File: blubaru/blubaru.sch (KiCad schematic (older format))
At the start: 20 parts

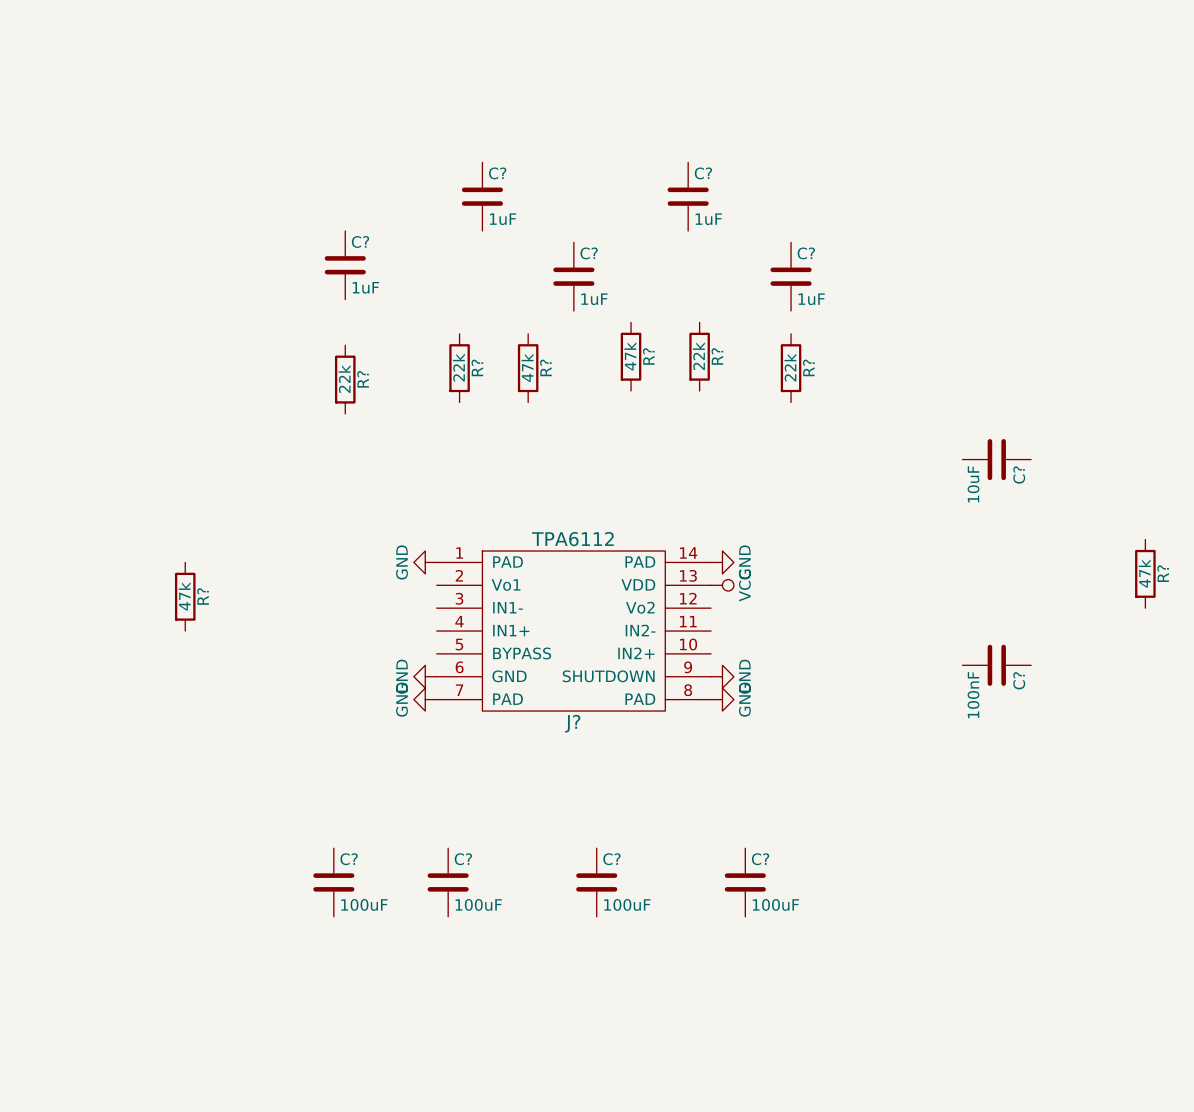
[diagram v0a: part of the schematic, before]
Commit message: Make connections to components on amplifier.
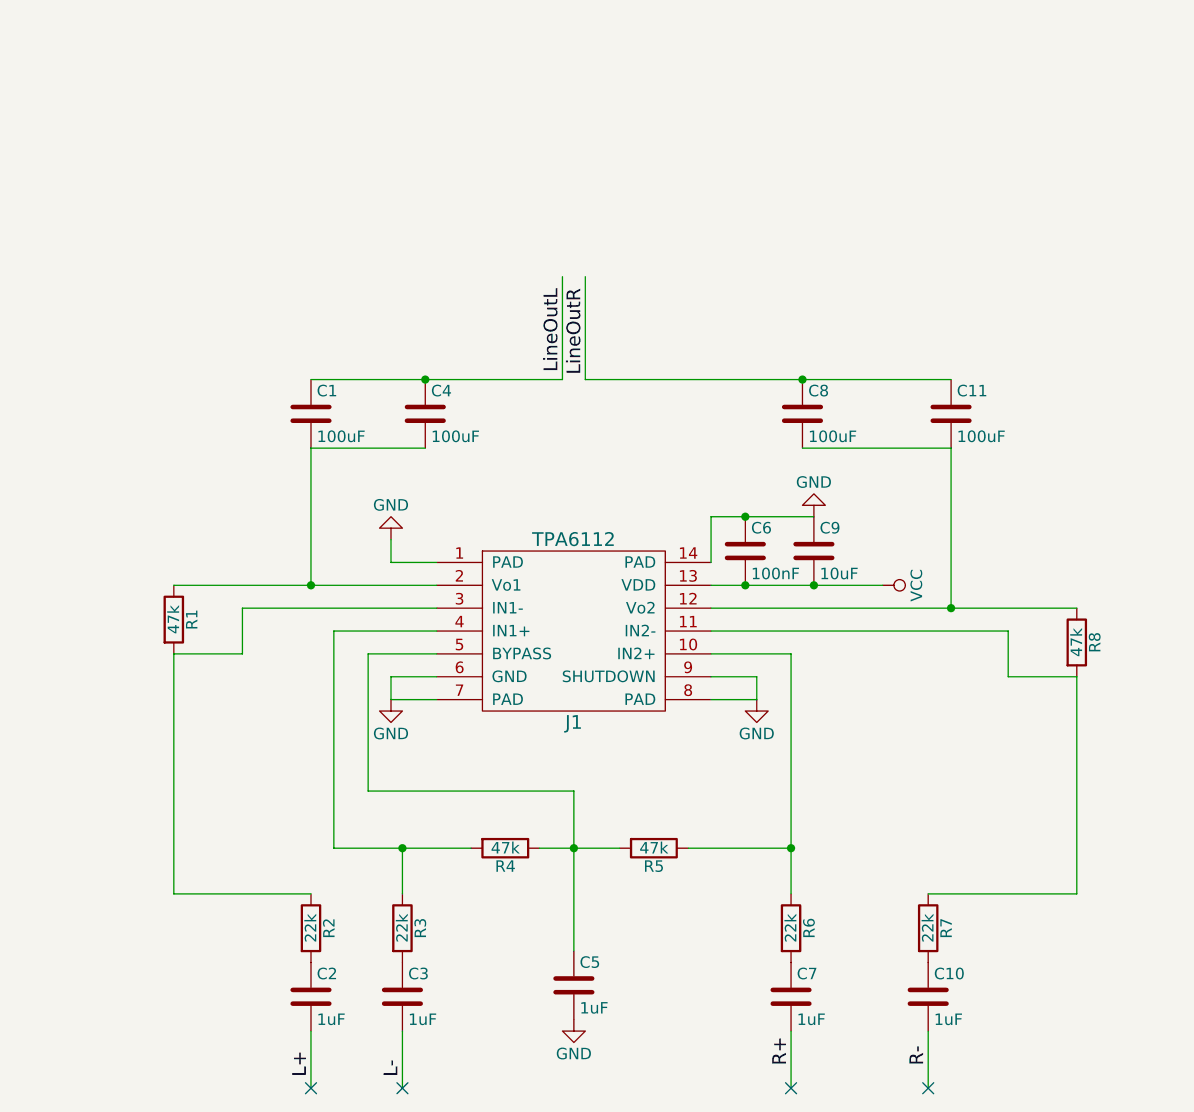
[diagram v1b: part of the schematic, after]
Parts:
- gave numbers to parts that had none: 20
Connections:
- net labels added: L+, L-, LineOutL, LineOutR, R+, R-
- wire segments 0 -> 47
- no-connect marks 0 -> 4
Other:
- moved on the sheet: C1, C10, C11, C2, C3, C4, C5, C6, C7, C8, C9, R1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

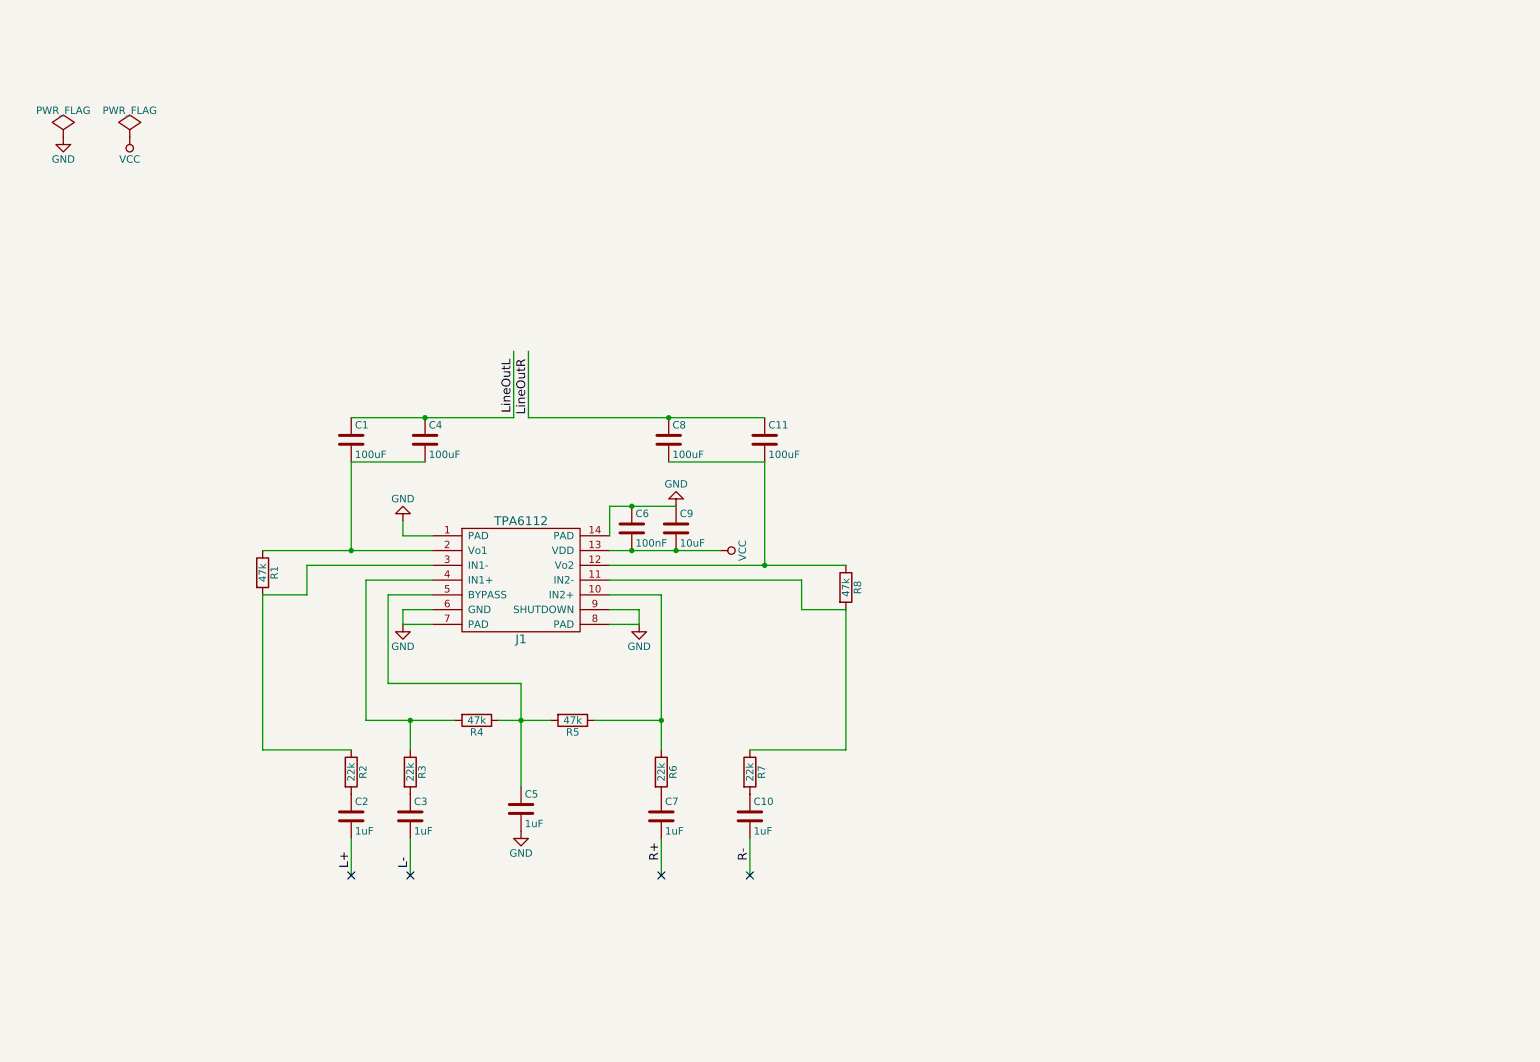
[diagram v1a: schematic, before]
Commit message: Add the RN52 to my library and schematic
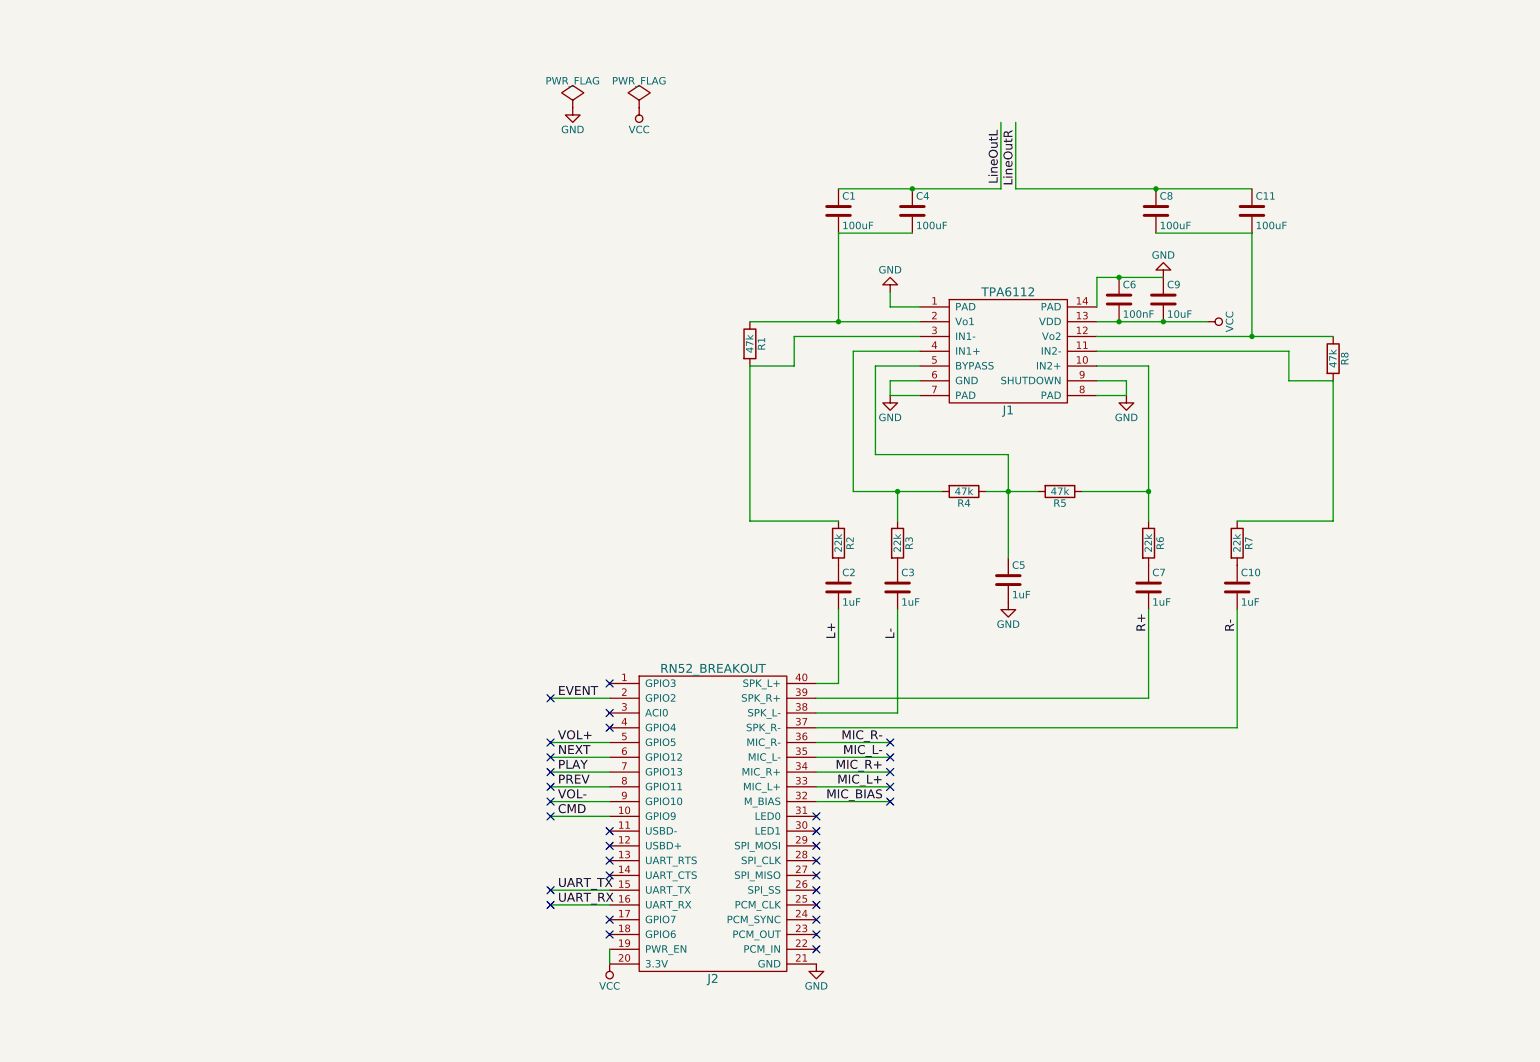
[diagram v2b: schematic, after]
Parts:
- added J2: RN52_BREAKOUT, symbol RN52_BREAKOUT
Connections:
- net labels added: CMD, EVENT, MIC_BIAS, MIC_L+, MIC_L-, MIC_R+, MIC_R-, NEXT, PLAY, PREV, UART_RX, UART_TX, VOL+, VOL-
- wire segments 47 -> 66
- no-connect marks 4 -> 33
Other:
- moved on the sheet: C1, C10, C11, C2, C3, C4, C5, C6, C7, C8, C9, J1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

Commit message: Add DB15s and a cap on the breakout.
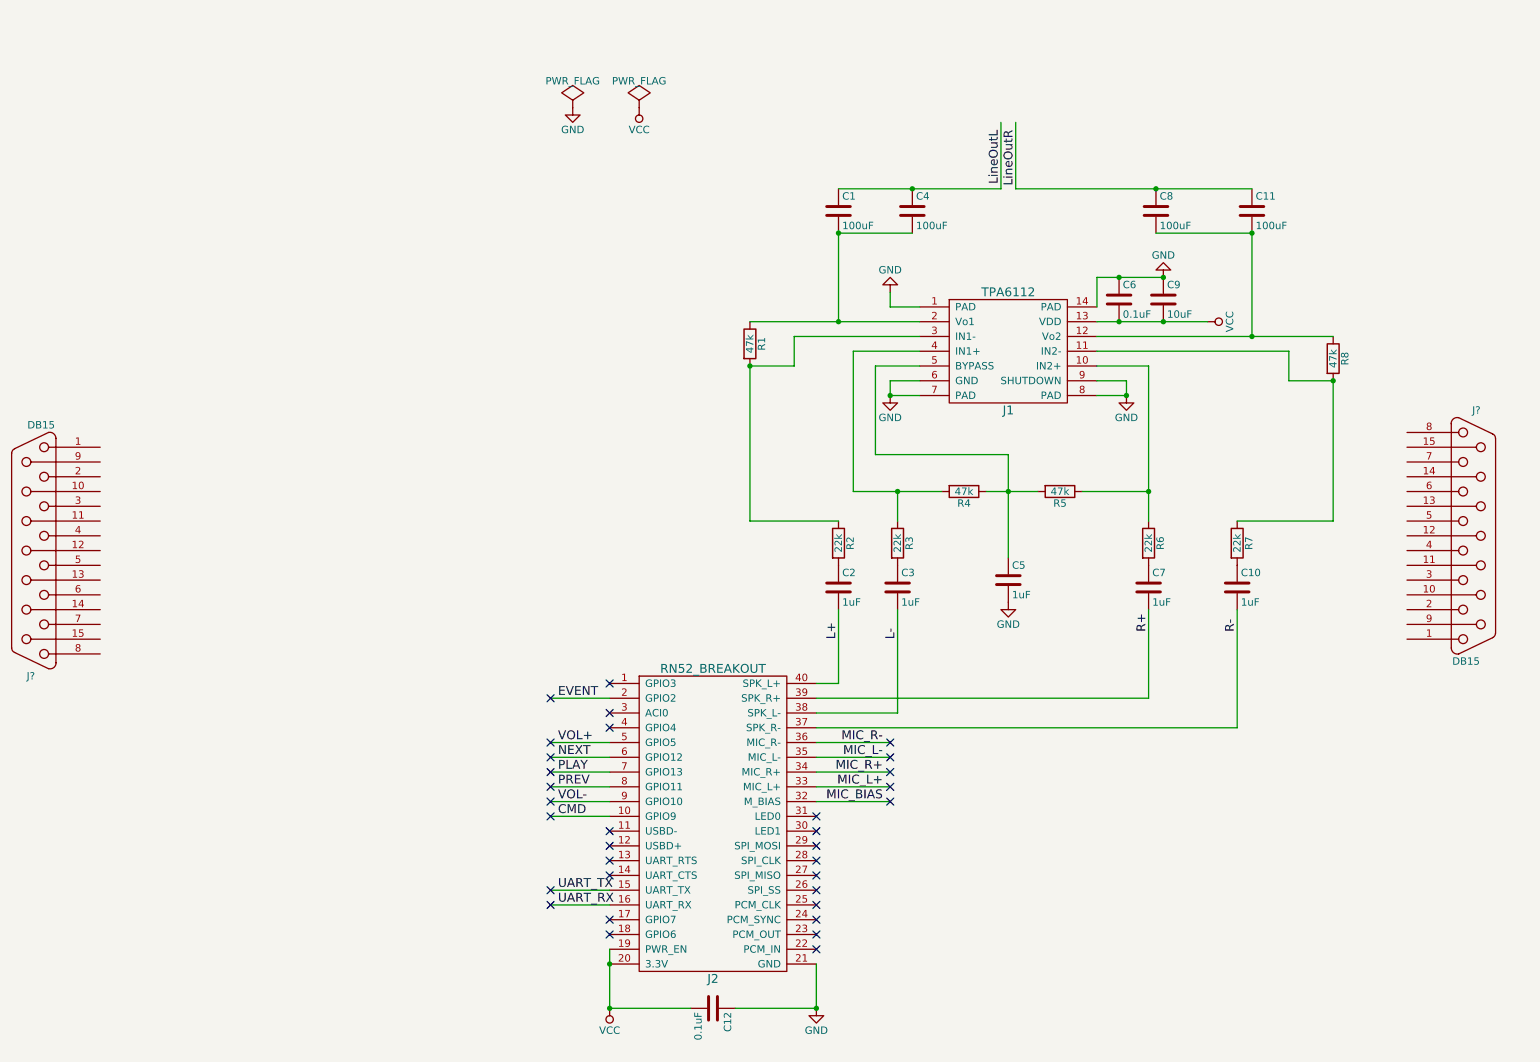
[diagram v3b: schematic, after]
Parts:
- added C12: 0.1uF, symbol C
- added J? (x2): DB15, symbol DB15
- C6: value 100nF -> 0.1uF
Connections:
- net GND: now also C12.1
- net VCC: now also C12.2
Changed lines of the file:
@@
 P 8200 2600
 F 0 "C6" H 8225 2700 50  0000 L CNN
-F 1 "100nF" H 8225 2500 50  0000 L CNN
+F 1 "0.1uF" H 8225 2500 50  0000 L CNN
 F 2 "" H 8238 2450 50  0000 C CNN
 F 3 "" H 8200 2600 50  0000 C CNN
@@
 $EndComp
 $Comp
-L GND #PWR01
+L GND #PWR9
 U 1 1 5899599A
 P 8500 2450
-F 0 "#PWR01" H 8500 2200 50  0001 C CNN
+F 0 "#PWR9" H 8500 2200 50  0001 C CNN
 F 1 "GND" H 8500 2300 50  0000 C CNN
 F 2 "" H 8500 2450 50  0000 C CNN
@@
 $EndComp
 $Comp
-L GND #PWR02
+L GND #PWR8
 U 1 1 589959D6
 P 8250 3250
-F 0 "#PWR02" H 8250 3000 50  0001 C CNN
+F 0 "#PWR8" H 8250 3000 50  0001 C CNN
 F 1 "GND" H 8250 3100 50  0000 C CNN
 F 2 "" H 8250 3250 50  0000 C CNN
@@
 $EndComp
 $Comp
-L GND #PWR03
+L GND #PWR5
 U 1 1 58995A12
 P 6650 2550
-F 0 "#PWR03" H 6650 2300 50  0001 C CNN
+F 0 "#PWR5" H 6650 2300 50  0001 C CNN
 F 1 "GND" H 6650 2400 50  0000 C CNN
 F 2 "" H 6650 2550 50  0000 C CNN
@@
 $EndComp
 $Comp
-L GND #PWR04
+L GND #PWR6
 U 1 1 58995A8A
 P 6650 3250
-F 0 "#PWR04" H 6650 3000 50  0001 C CNN
+F 0 "#PWR6" H 6650 3000 50  0001 C CNN
 F 1 "GND" H 6650 3100 50  0000 C CNN
 F 2 "" H 6650 3250 50  0000 C CNN
@@
 $EndComp
 $Comp
-L PWR_FLAG #FLG05
+L PWR_FLAG #FLG1
 U 1 1 58995B8E
 P 4500 1300
-F 0 "#FLG05" H 4500 1395 50  0001 C CNN
+F 0 "#FLG1" H 4500 1395 50  0001 C CNN
 F 1 "PWR_FLAG" H 4500 1480 50  0000 C CNN
 F 2 "" H 4500 1300 50  0000 C CNN
@@
 $EndComp
 $Comp
-L PWR_FLAG #FLG06
+L PWR_FLAG #FLG2
 U 1 1 58995BDE
 P 4950 1300
-F 0 "#FLG06" H 4950 1395 50  0001 C CNN
+F 0 "#FLG2" H 4950 1395 50  0001 C CNN
 F 1 "PWR_FLAG" H 4950 1480 50  0000 C CNN
 F 2 "" H 4950 1300 50  0000 C CNN
@@
 $EndComp
 $Comp
-L GND #PWR07
+L GND #PWR1
 U 1 1 58995C7E
 P 4500 1300
-F 0 "#PWR07" H 4500 1050 50  0001 C CNN
+F 0 "#PWR1" H 4500 1050 50  0001 C CNN
 F 1 "GND" H 4500 1150 50  0000 C CNN
 F 2 "" H 4500 1300 50  0000 C CNN
@@
 $EndComp
 $Comp
-L VCC #PWR08
+L VCC #PWR3
 U 1 1 58995CE2
 P 4950 1300
-F 0 "#PWR08" H 4950 1150 50  0001 C CNN
+F 0 "#PWR3" H 4950 1150 50  0001 C CNN
 F 1 "VCC" H 4950 1450 50  0000 C CNN
 F 2 "" H 4950 1300 50  0000 C CNN
@@
 $EndComp
 $Comp
-L VCC #PWR09
+L VCC #PWR10
 U 1 1 589A8C5A
 P 8800 2750
-F 0 "#PWR09" H 8800 2600 50  0001 C CNN
+F 0 "#PWR10" H 8800 2600 50  0001 C CNN
 F 1 "VCC" H 8800 2900 50  0000 C CNN
 F 2 "" H 8800 2750 50  0000 C CNN
@@
 LineOutL
 $Comp
-L GND #PWR010
+L GND #PWR7
 U 1 1 589AA8CC
 P 7450 4650
-F 0 "#PWR010" H 7450 4400 50  0001 C CNN
+F 0 "#PWR7" H 7450 4400 50  0001 C CNN
 F 1 "GND" H 7450 4500 50  0000 C CNN
 F 2 "" H 7450 4650 50  0000 C CNN
@@
 $EndComp
 $Comp
-L GND #PWR011
+L GND #PWR4
 U 1 1 589AA392
-P 6150 7100
-F 0 "#PWR011" H 6150 6850 50  0001 C CNN
-F 1 "GND" H 6150 6950 50  0000 C CNN
-F 2 "" H 6150 7100 50  0000 C CNN
-F 3 "" H 6150 7100 50  0000 C CNN
-	1    6150 7100
-	1    0    0    -1
-$EndComp
-$Comp
-L VCC #PWR012
+P 6150 7400
+F 0 "#PWR4" H 6150 7150 50  0001 C CNN
+F 1 "GND" H 6150 7250 50  0000 C CNN
+F 2 "" H 6150 7400 50  0000 C CNN
+F 3 "" H 6150 7400 50  0000 C CNN
+	1    6150 7400
+	1    0    0    -1
+$EndComp
+$Comp
+L VCC #PWR2
 U 1 1 589AA3E5
-P 4750 7100
-F 0 "#PWR012" H 4750 6950 50  0001 C CNN
-F 1 "VCC" H 4750 7250 50  0000 C CNN
-F 2 "" H 4750 7100 50  0000 C CNN
-F 3 "" H 4750 7100 50  0000 C CNN
-	1    4750 7100
+P 4750 7400
+F 0 "#PWR2" H 4750 7250 50  0001 C CNN
+F 1 "VCC" H 4750 7550 50  0000 C CNN
+F 2 "" H 4750 7400 50  0000 C CNN
+F 3 "" H 4750 7400 50  0000 C CNN
+	1    4750 7400
 	-1   0    0    1
 $EndComp
@@
 Connection ~ 8500 2750
 Wire Wire Line
-	4750 7000 4750 7100
+	4750 7000 4750 7400
 Wire Wire Line
 	6300 5200 6150 5200
@@
 NoConn ~ 6650 5900
 NoConn ~ 6650 6000
+Connection ~ 4750 7100
+Connection ~ 8250 3250
+Connection ~ 6650 3250
+Connection ~ 5700 3050
+Connection ~ 9650 3150
+Connection ~ 9100 2150
+Connection ~ 6300 2150
+Connection ~ 8500 2450
+$Comp
+L C C12
+U 1 1 589BA198
+P 5450 7400
+F 0 "C12" H 5475 7500 50  0000 L CNN
+F 1 "0.1uF" H 5475 7300 50  0000 L CNN
+F 2 "" H 5488 7250 50  0000 C CNN
+F 3 "" H 5450 7400 50  0000 C CNN
+	1    5450 7400
+	0    1    1    0
+$EndComp
+Wire Wire Line
+	6150 7100 6150 7400
+Wire Wire Line
+	6150 7400 5600 7400
+Wire Wire Line
+	4750 7400 5300 7400
+Connection ~ 6150 7400
+Connection ~ 4750 7400
+$Comp
+L DB15 J?
+U 1 1 589BBD0D
+P 10600 4200
+F 0 "J?" H 10620 5050 50  0000 C CNN
+F 1 "DB15" H 10550 3350 50  0000 C CNN
+F 2 "" H 10600 4200 50  0000 C CNN
+F 3 "" H 10600 4200 50  0000 C CNN
+	1    10600 4200
+	1    0    0    -1
+$EndComp
+$Comp
+L DB15 J?
+U 1 1 589BBD68
+P 850 4300
+F 0 "J?" H 870 5150 50  0000 C CNN
+F 1 "DB15" H 800 3450 50  0000 C CNN
+F 2 "" H 850 4300 50  0000 C CNN
+F 3 "" H 850 4300 50  0000 C CNN
+	1    850  4300
+	-1   0    0    1
+$EndComp
 $EndSCHEMATC
